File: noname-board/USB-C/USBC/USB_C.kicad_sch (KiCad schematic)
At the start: 10 parts, among them J2 USB_C_Receptacle, U4 AP2112K-3.3

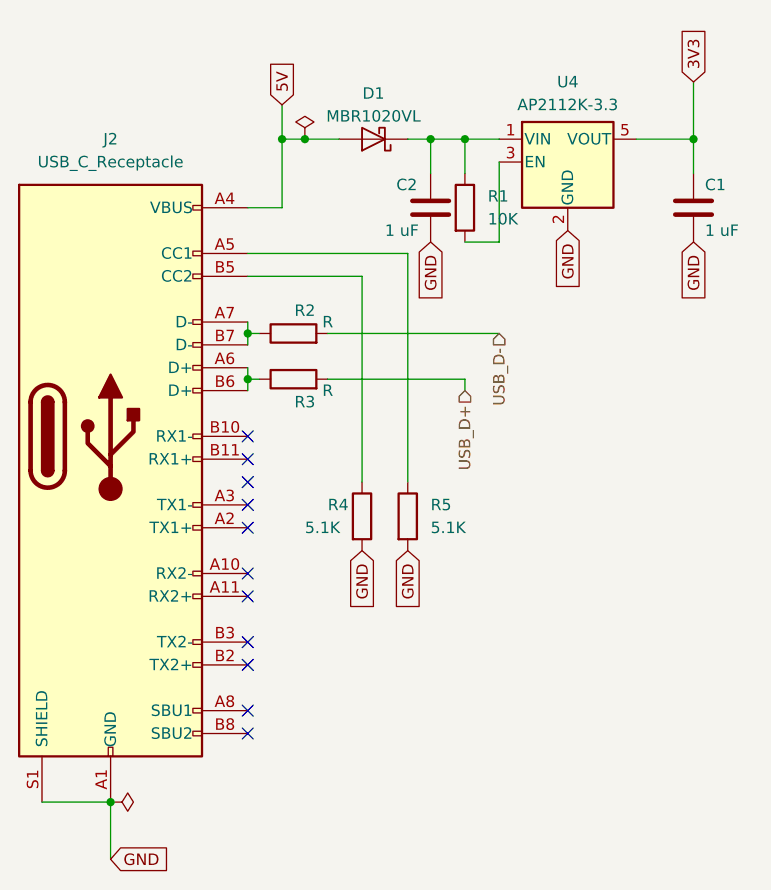
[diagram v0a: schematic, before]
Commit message: Changed Global to Hierarchals
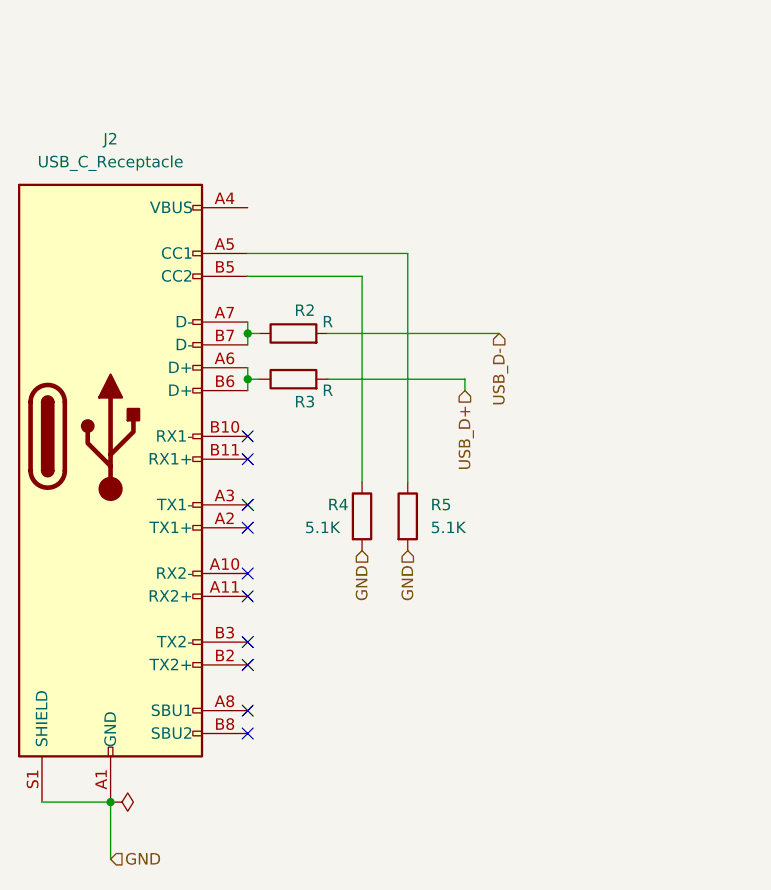
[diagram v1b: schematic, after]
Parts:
- removed C1, C2: 1 uF, Capacitor_THT:CP_Axial_L10.0mm_D4.5mm_P15.00mm_Horizontal, symbol Device:C
- removed D1: MBR1020VL, Diode_SMD:D_SOD-123F, symbol Diode:MBR1020VL
- removed R1: 10K, Resistor_THT:R_Axial_DIN0207_L6.3mm_D2.5mm_P10.16mm_Horizontal, symbol Device:R
- removed U4: AP2112K-3.3, Package_TO_SOT_SMD:SOT-23-5, symbol Regulator_Linear:AP2112K-3.3
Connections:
- net 5V: no longer names the net of J2.A4 (VBUS), J2.A9 (VBUS), J2.B4 (VBUS), J2.B9 (VBUS)
- no-connect marks 11 -> 10

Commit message: Did Stuff
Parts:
- removed R2, R3: R, Resistor_THT:R_Axial_DIN0207_L6.3mm_D2.5mm_P10.16mm_Horizontal, symbol Device:R
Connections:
- net USB_D+: now also J2.A6 (D+), J2.B6 (D+)
- net USB_D-: now also J2.A7 (D-), J2.B7 (D-)
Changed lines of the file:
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@@
     (stroke (width 0) (type default))
   )
-  (wire (pts (xy 92.71 83.82) (xy 91.44 83.82))
+  (wire (pts (xy 91.44 83.82) (xy 119.38 83.82))
     (stroke (width 0) (type default))
   )
   (wire (pts (xy 91.44 83.82) (xy 91.44 85.09))
+    (stroke (width 0) (type default))
+  )
+  (wire (pts (xy 91.44 88.9) (xy 115.57 88.9))
     (stroke (width 0) (type default))
   )
@@
     (stroke (width 0) (type default))
   )
-  (wire (pts (xy 100.33 88.9) (xy 115.57 88.9))
-    (stroke (width 0) (type default))
-  )
   (wire (pts (xy 91.44 88.9) (xy 91.44 90.17))
-    (stroke (width 0) (type default))
-  )
-  (wire (pts (xy 92.71 88.9) (xy 91.44 88.9))
-    (stroke (width 0) (type default))
-  )
-  (wire (pts (xy 119.38 83.82) (xy 100.33 83.82))
     (stroke (width 0) (type default))
   )
@@
     )
   )
-  (symbol (lib_id "Device:R") (at 96.52 83.82 90) (unit 1)
-    (in_bom yes) (on_board yes) (dnp no)
-    (property "Reference" "R2" (at 97.79 81.28 90)
-      (effects (font (size 1.27 1.27)))
-    )
-    (property "Value" "R" (at 100.33 82.55 90)
-      (effects (font (size 1.27 1.27)))
-    )
-    (property "Footprint" "Resistor_THT:R_Axial_DIN0207_L6.3mm_D2.5mm_P10.16mm_Horizontal" (at 96.52 85.598 90)
-      (effects (font (size 1.27 1.27)) hide)
-    )
-    (property "Datasheet" "~" (at 96.52 83.82 0)
-      (effects (font (size 1.27 1.27)) hide)
-    )
-    (pin "1")
-    (pin "2")
-    (instances
-      (project "USBC"
-        (path "/f2e74a7f-7065-4b2f-90db-12a09c16d2ca"
-          (reference "R2") (unit 1)
-        )
-        (path "/f2e74a7f-7065-4b2f-90db-12a09c16d2ca/2f5bc9a6-e62f-4fad-b6eb-0074f3852e7e"
-          (reference "R6") (unit 1)
-        )
-      )
-    )
-  )
   (symbol (lib_id "Device:R") (at 104.14 104.14 0) (unit 1)
     (in_bom yes) (on_board yes) (dnp no)
@@
         )
       )
-    )
-  )
-  (symbol (lib_id "Device:R") (at 96.52 88.9 90) (unit 1)
-    (in_bom yes) (on_board yes) (dnp no)
-    (property "Reference" "R3" (at 97.79 91.44 90)
-      (effects (font (size 1.27 1.27)))
-    )
-    (property "Value" "R" (at 100.33 90.17 90)
-      (effects (font (size 1.27 1.27)))
-    )
-    (property "Footprint" "Resistor_THT:R_Axial_DIN0207_L6.3mm_D2.5mm_P10.16mm_Horizontal" (at 96.52 90.678 90)
-      (effects (font (size 1.27 1.27)) hide)
-    )
-    (property "Datasheet" "~" (at 96.52 88.9 0)
-      (effects (font (size 1.27 1.27)) hide)
-    )
-    (pin "1")
-    (pin "2")
-    (instances
-      (project "USBC"
-        (path "/f2e74a7f-7065-4b2f-90db-12a09c16d2ca"
-          (reference "R3") (unit 1)
-        )
-        (path "/f2e74a7f-7065-4b2f-90db-12a09c16d2ca/2f5bc9a6-e62f-4fad-b6eb-0074f3852e7e"
-          (reference "R7") (unit 1)
-        )
-      )
